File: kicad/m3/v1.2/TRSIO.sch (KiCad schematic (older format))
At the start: 25 parts, among them J1 TRS80, J2 +5V, J3 BUTTON, J4 LED, J5 FreHD Disable, J6 TRS80, Q1 2N7000, Q2 2N7000, Q3 2N7000, SW1 SW_Push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

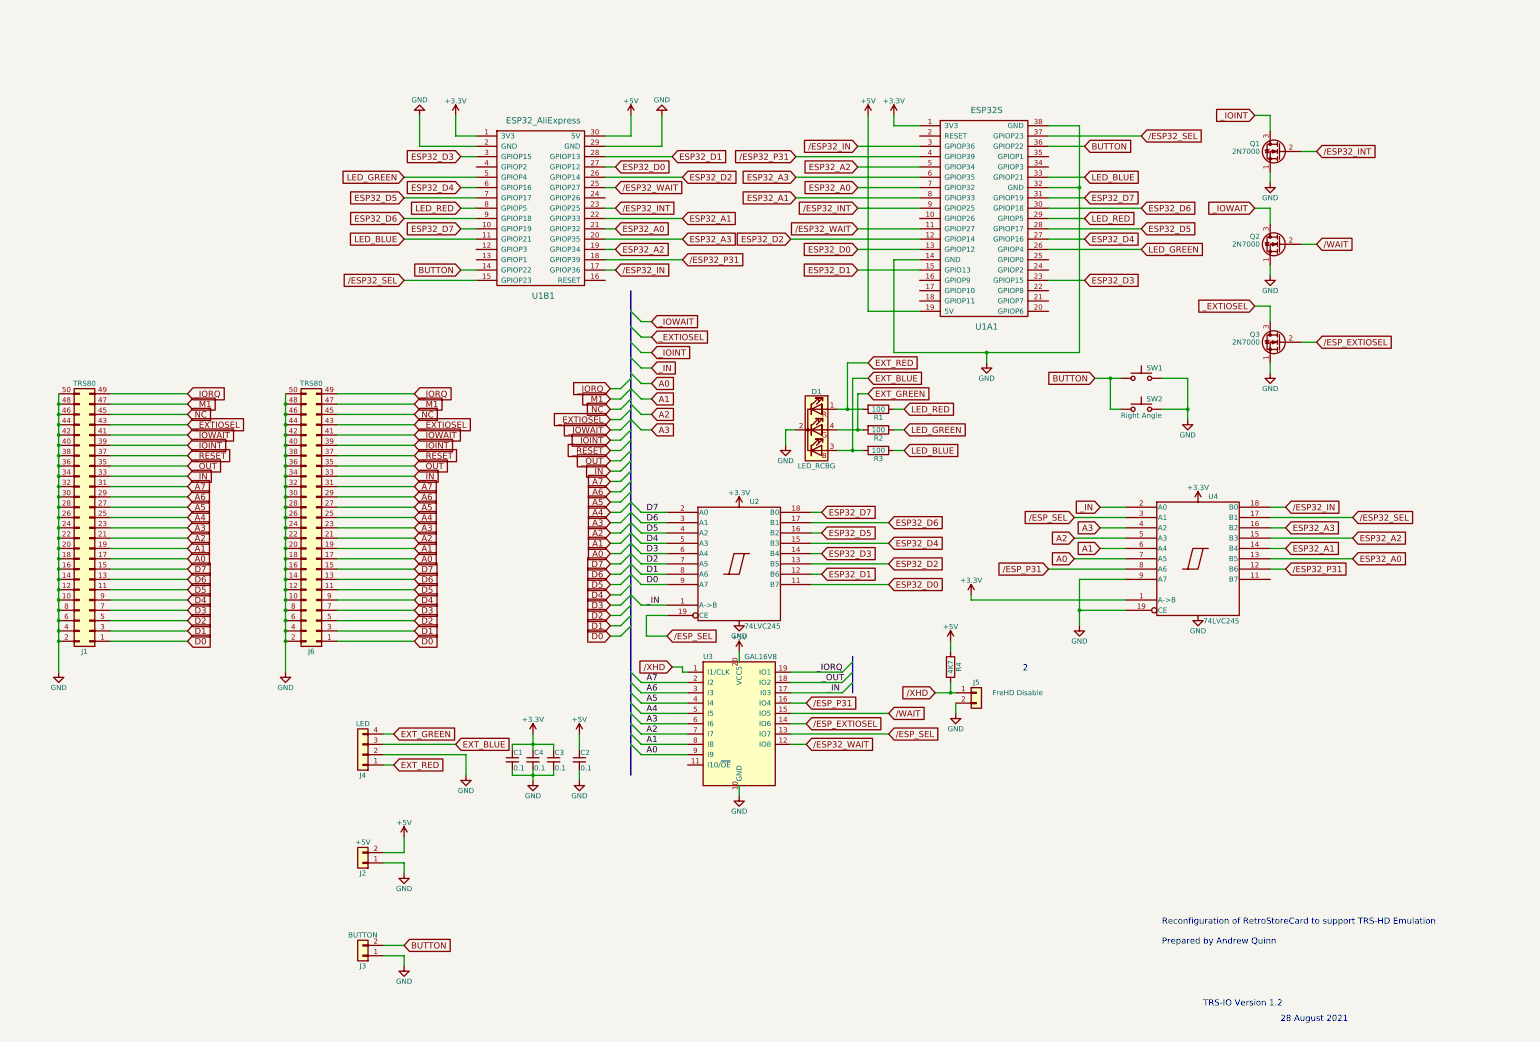
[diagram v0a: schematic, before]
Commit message: TRS-IO-M3 PCB v1.2 + SD Card
Schematic updates only.  PCB still outstanding
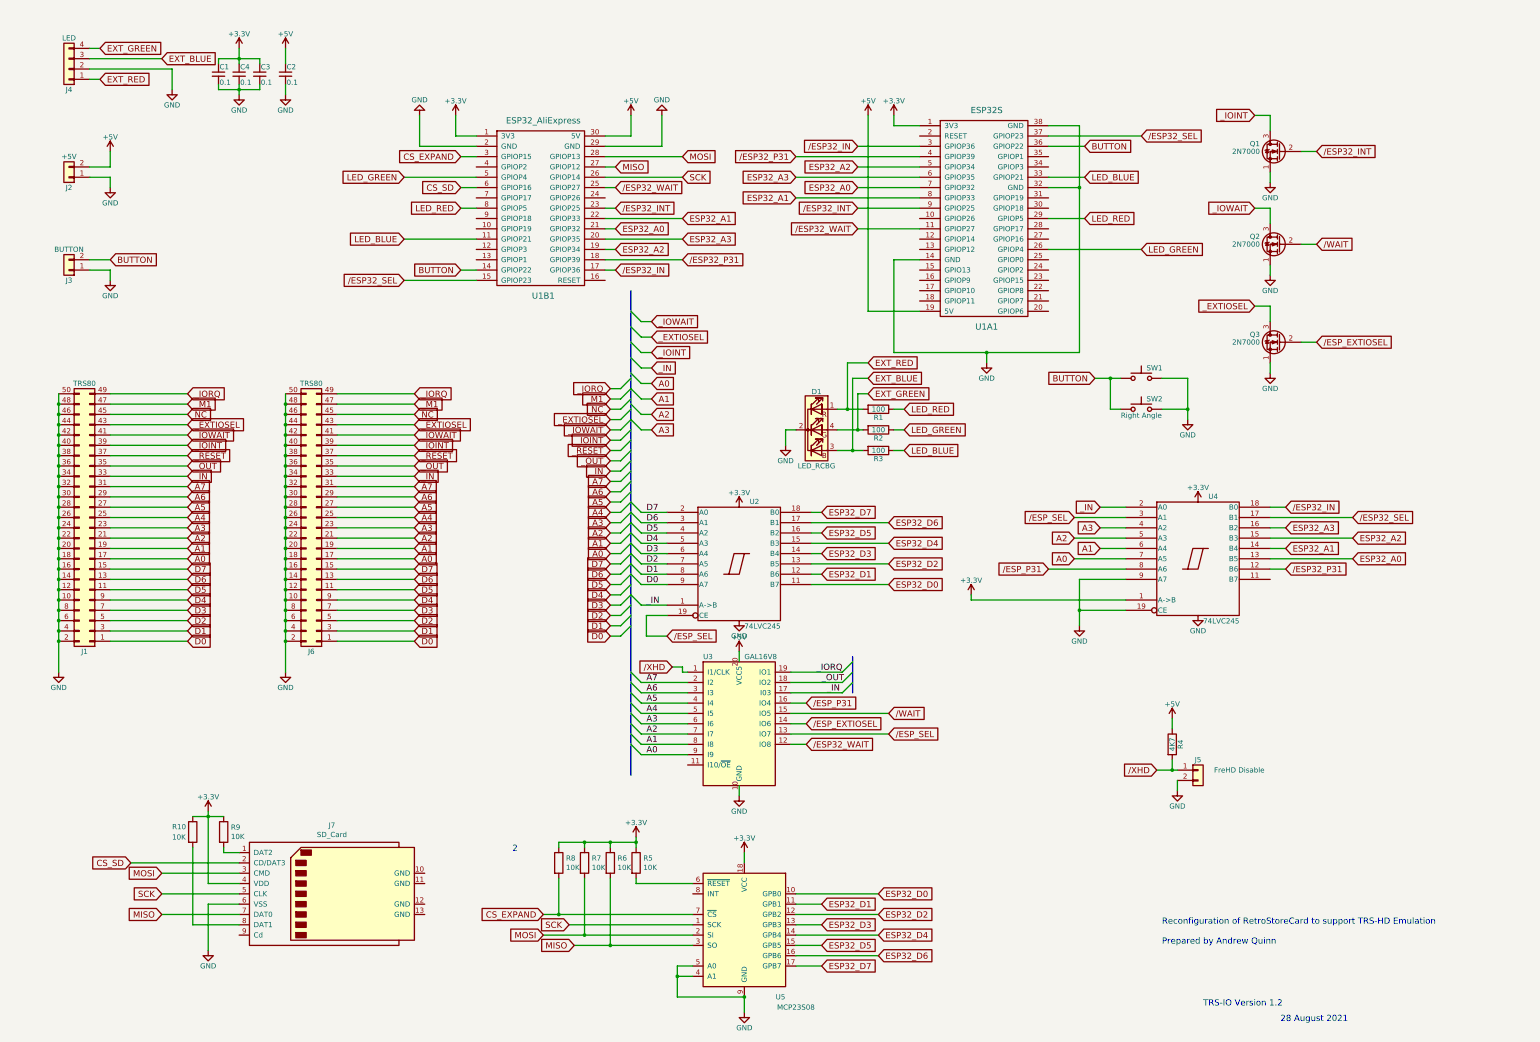
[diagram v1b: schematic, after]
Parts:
- added J7: SD_Card, symbol SDCard:SD_Card
- added R10, R5, R6, R7, R8, R9: 10K, symbol Device:R
- added U5: MCP23S08, symbol microchip:MCP23S08
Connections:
- net +3V3: now also J7.4 (VDD), R10.1, R5.1, R6.1, R7.1, R8.1, R9.1, U5.18 (VCC)
- net ESP32_D0: now also U5.10 (GPB0); no longer U1A1.13 (GPIOP12), U1B1.27 (GPIOP12)
- net ESP32_D1: now also U5.11 (GPB1); no longer U1A1.15 (GPIO13), U1B1.28 (GPIOP13)
- net ESP32_D2: now also U5.12 (GPB2); no longer U1A1.12 (GPIOP14), U1B1.26 (GPIOP14)
- net ESP32_D3: now also U5.13 (GPB3); no longer U1A1.23 (GPIOP15), U1B1.3 (GPIOP15)
- net ESP32_D4: now also U5.14 (GPB4); no longer U1A1.27 (GPIOP16), U1B1.6 (GPIOP16)
- net ESP32_D5: now also U5.15 (GPB5); no longer U1A1.28 (GPIOP17), U1B1.7 (GPIOP17)
- net ESP32_D6: now also U5.16 (GPB6); no longer U1A1.30 (GPIOP18), U1B1.9 (GPIOP18)
- net ESP32_D7: now also U5.17 (GPB7); no longer U1A1.31 (GPIOP19), U1B1.10 (GPIOP19)
- net GND: now also J7.6 (VSS), U5.4 (A1), U5.5 (A0), U5.9 (GND)
- new net: R5.2, U5.6 (~RESET)
- new net: J7.1 (DAT2), R9.2
- new net: J7.8 (DAT1), R10.2
- new net CS_EXPAND: R8.2, U1B1.3 (GPIOP15), U5.7 (~CS)
- new net CS_SD: J7.2 (CD/DAT3), U1B1.6 (GPIOP16)
- new net MISO: J7.7 (DAT0), R6.2, U1B1.27 (GPIOP12), U5.3 (SO)
- new net MOSI: J7.3 (CMD), R7.2, U1B1.28 (GPIOP13), U5.2 (SI)
- new net SCK: J7.5 (CLK), U1B1.26 (GPIOP14), U5.1 (SCK)
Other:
- moved on the sheet: C1, C2, C3, C4, J2, J3, J4, J5, R4

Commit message: TRS-IO-M3 PCB v1.2 + SD Card + PCB Updates
1. Connect GND pins of the SD card to ground
2. SPI pins connected for ESP32S
3. Pullup for CS_SD
4. PCB Layout
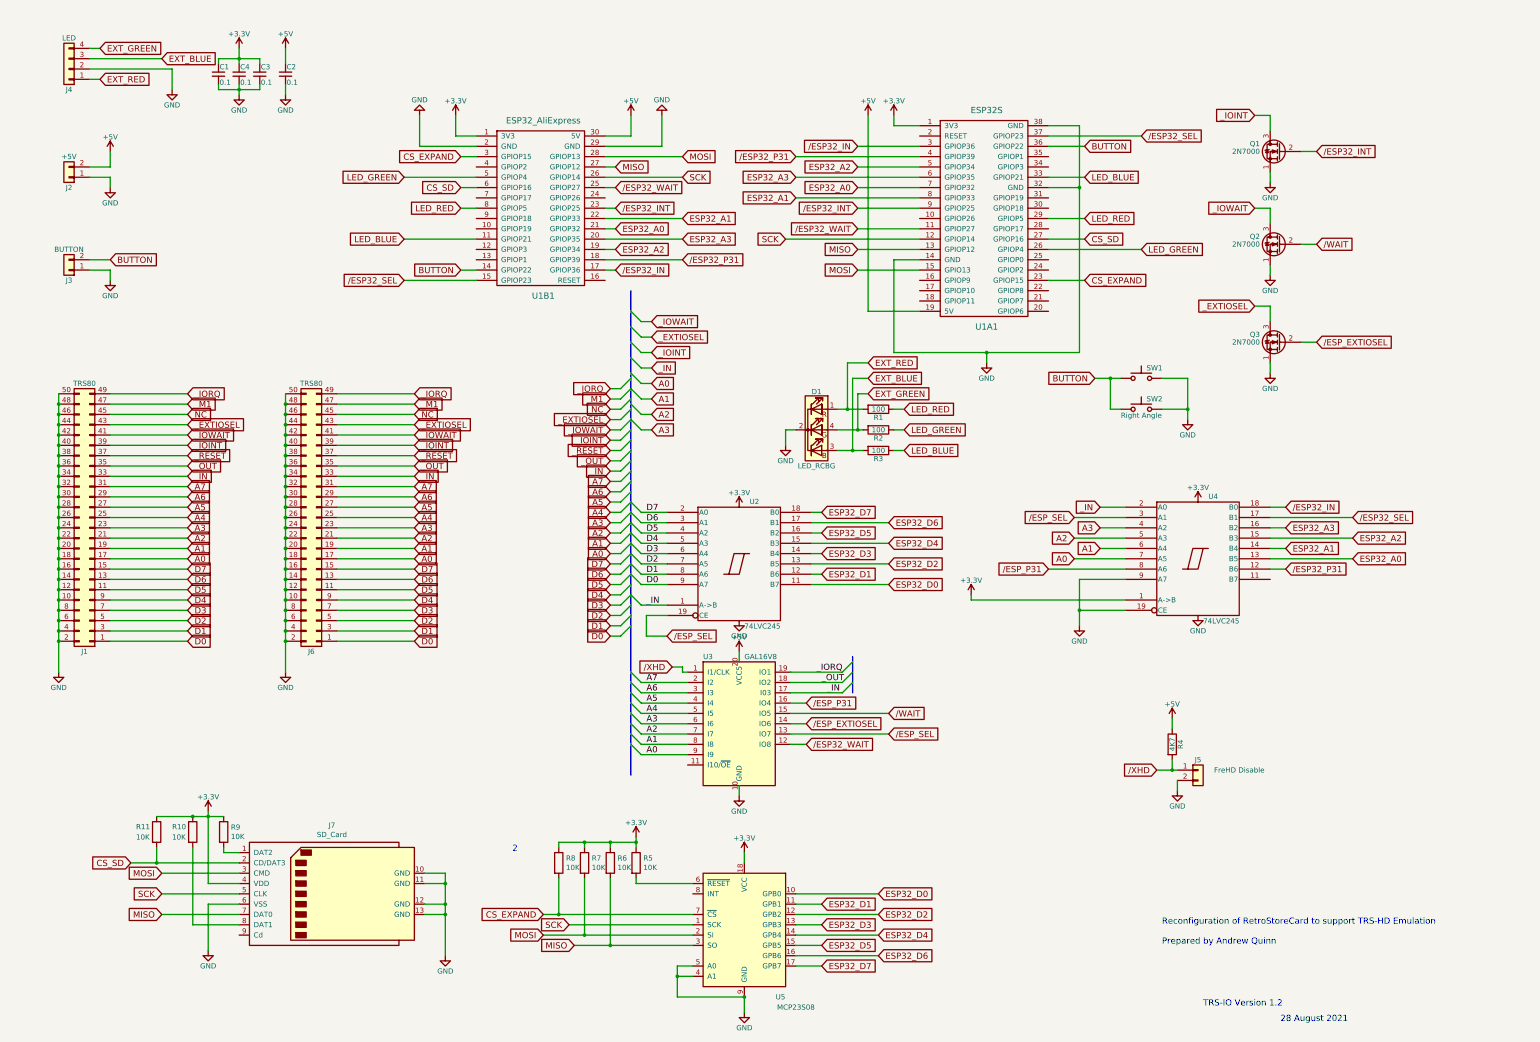
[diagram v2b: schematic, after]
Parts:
- added R11: 10K, Resistors_THT:R_Axial_DIN0207_L6.3mm_D2.5mm_P7.62mm_Horizontal, symbol Device:R
- J7: footprint (none) -> TRSIO:TFP09-2-12B
- R10, R5, R6, R7, R8, R9: footprint (none) -> Resistors_THT:R_Axial_DIN0207_L6.3mm_D2.5mm_P7.62mm_Horizontal
- U5: footprint (none) -> Housings_DIP:DIP-18_W7.62mm
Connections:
- net +3V3: now also R11.1
- net CS_EXPAND: now also U1A1.23 (GPIOP15)
- net CS_SD: now also U1A1.27 (GPIOP16), R11.2
- net GND: now also J7.10 (GND), J7.11 (GND), J7.12 (GND), J7.13 (GND)
- net MISO: now also U1A1.13 (GPIOP12)
- net MOSI: now also U1A1.15 (GPIO13)
- net SCK: now also U1A1.12 (GPIOP14)
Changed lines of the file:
@@
 F 0 "U5" H 7550 9400 50  0000 C CNN
 F 1 "MCP23S08" H 7400 9300 50  0000 C CNN
-F 2 "" H 7950 9450 50  0001 L CNN
+F 2 "Housings_DIP:DIP-18_W7.62mm" H 7950 9450 50  0001 L CNN
 F 3 "http://ww1.microchip.com/downloads/en/DeviceDoc/21919e.pdf" H 8150 10700 50  0001 C CNN
 	1    7900 10100
@@
 F 0 "R5" H 6920 9546 50  0000 L CNN
 F 1 "10K" H 6920 9455 50  0000 L CNN
-F 2 "" V 6780 9500 50  0001 C CNN
+F 2 "Resistors_THT:R_Axial_DIN0207_L6.3mm_D2.5mm_P7.62mm_Horizontal" V 6780 9500 50  0001 C CNN
 F 3 "~" H 6850 9500 50  0001 C CNN
 	1    6850 9500
@@
 F 0 "R6" H 6670 9546 50  0000 L CNN
 F 1 "10K" H 6670 9455 50  0000 L CNN
-F 2 "" V 6530 9500 50  0001 C CNN
+F 2 "Resistors_THT:R_Axial_DIN0207_L6.3mm_D2.5mm_P7.62mm_Horizontal" V 6530 9500 50  0001 C CNN
 F 3 "~" H 6600 9500 50  0001 C CNN
 	1    6600 9500
@@
 F 0 "R7" H 6420 9546 50  0000 L CNN
 F 1 "10K" H 6420 9455 50  0000 L CNN
-F 2 "" V 6280 9500 50  0001 C CNN
+F 2 "Resistors_THT:R_Axial_DIN0207_L6.3mm_D2.5mm_P7.62mm_Horizontal" V 6280 9500 50  0001 C CNN
 F 3 "~" H 6350 9500 50  0001 C CNN
 	1    6350 9500
@@
 F 0 "R8" H 6170 9546 50  0000 L CNN
 F 1 "10K" H 6170 9455 50  0000 L CNN
-F 2 "" V 6030 9500 50  0001 C CNN
+F 2 "Resistors_THT:R_Axial_DIN0207_L6.3mm_D2.5mm_P7.62mm_Horizontal" V 6030 9500 50  0001 C CNN
 F 3 "~" H 6100 9500 50  0001 C CNN
 	1    6100 9500
@@
 F 0 "J7" H 3900 10465 50  0000 C CNN
 F 1 "SD_Card" H 3900 10374 50  0000 C CNN
-F 2 "" H 3900 9800 50  0001 C CNN
+F 2 "TRSIO:TFP09-2-12B" H 3900 9800 50  0001 C CNN
 F 3 "http://portal.fciconnect.com/Comergent//fci/drawing/10067847.pdf" H 3900 9800 50  0001 C CNN
 	1    3900 9800
@@
 F 0 "R9" H 2920 9246 50  0000 L CNN
 F 1 "10K" H 2920 9155 50  0000 L CNN
-F 2 "" V 2780 9200 50  0001 C CNN
+F 2 "Resistors_THT:R_Axial_DIN0207_L6.3mm_D2.5mm_P7.62mm_Horizontal" V 2780 9200 50  0001 C CNN
 F 3 "~" H 2850 9200 50  0001 C CNN
 	1    2850 9200
@@
 SCK
 Wire Wire Line
-	1950 9500 3000 9500
+	1950 9500 2200 9500
 Wire Wire Line
 	2250 9600 3000 9600
@@
 F 0 "R10" H 2350 9250 50  0000 L CNN
 F 1 "10K" H 2350 9150 50  0000 L CNN
-F 2 "" V 2480 9200 50  0001 C CNN
+F 2 "Resistors_THT:R_Axial_DIN0207_L6.3mm_D2.5mm_P7.62mm_Horizontal" V 2480 9200 50  0001 C CNN
 F 3 "~" H 2550 9200 50  0001 C CNN
 	1    2550 9200
@@
 Wire Wire Line
 	2700 9900 2700 10350
+Text GLabel 11200 3850 2    60   Input ~ 0
+CS_EXPAND
+Wire Wire Line
+	10850 3850 11200 3850
+Text GLabel 11200 3450 2    60   Input ~ 0
+CS_SD
+Wire Wire Line
+	11200 3450 10850 3450
+Text GLabel 9000 3750 0    60   Input ~ 0
+MOSI
+Wire Wire Line
+	9600 3750 9000 3750
+Text GLabel 9000 3550 0    60   Input ~ 0
+MISO
+Wire Wire Line
+	9000 3550 9600 3550
+Text GLabel 8300 3450 0    60   Input ~ 0
+SCK
+Wire Wire Line
+	8300 3450 9600 3450
+$Comp
+L Device:R R11
+U 1 1 61473039
+P 2200 9200
+F 0 "R11" H 2000 9250 50  0000 L CNN
+F 1 "10K" H 2000 9150 50  0000 L CNN
+F 2 "Resistors_THT:R_Axial_DIN0207_L6.3mm_D2.5mm_P7.62mm_Horizontal" V 2130 9200 50  0001 C CNN
+F 3 "~" H 2200 9200 50  0001 C CNN
+	1    2200 9200
+	1    0    0    -1
+$EndComp
+Wire Wire Line
+	2200 9050 2550 9050
+Connection ~ 2550 9050
+Wire Wire Line
+	2200 9350 2200 9500
+Connection ~ 2200 9500
+Wire Wire Line
+	2200 9500 3000 9500
+$Comp
+L power:GND #PWR?
+U 1 1 614CC471
+P 5000 10400
+F 0 "#PWR?" H 5000 10150 50  0001 C CNN
+F 1 "GND" H 5000 10250 50  0000 C CNN
+F 2 "" H 5000 10400 50  0001 C CNN
+F 3 "" H 5000 10400 50  0001 C CNN
+	1    5000 10400
+	1    0    0    -1
+$EndComp
+Wire Wire Line
+	4800 9600 5000 9600
+Wire Wire Line
+	5000 9600 5000 9700
+Wire Wire Line
+	4800 9700 5000 9700
+Connection ~ 5000 9700
+Wire Wire Line
+	5000 9700 5000 9900
+Wire Wire Line
+	4800 9900 5000 9900
+Connection ~ 5000 9900
+Wire Wire Line
+	5000 9900 5000 10000
+Wire Wire Line
+	4800 10000 5000 10000
 Wire Bus Line
 	8950 7500 8950 7850
 Wire Bus Line
 	6800 3950 6800 8650
+Connection ~ 5000 10000
+Wire Wire Line
+	5000 10000 5000 10400
 $EndSCHEMATC

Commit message: TRS-IO-M3 PCB v1.2 + SD Card + PCB Updates
1. Updated labels for buffered data bus signals from ESP32_Dx to BDx.
2. Updated meta data on schematic and PCB
3. Added M3 mounting holes to PCB
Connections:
- net ESP32_D0 renamed BD0
- net ESP32_D1 renamed BD1
- net ESP32_D2 renamed BD2
- net ESP32_D3 renamed BD3
- net ESP32_D4 renamed BD4
- net ESP32_D5 renamed BD5
- net ESP32_D6 renamed BD6
- net ESP32_D7 renamed BD7
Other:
- note added: "Updated TRS-IO with SD Card Support and Edge Connector"
- note removed: "Reconfiguration of RetroStoreCard to support TRS-HD Emulation\n\nPrepared by Andrew Quinn"
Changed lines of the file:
@@
 $EndComp
 Text GLabel 8650 6100 2    60   Input ~ 0
-ESP32_D7
+BD7
 Text GLabel 8650 6300 2    60   Input ~ 0
-ESP32_D5
+BD5
 Text GLabel 8650 6500 2    60   Input ~ 0
-ESP32_D3
+BD3
 Text GLabel 8650 6700 2    60   Input ~ 0
-ESP32_D1
+BD1
 Text GLabel 9300 6200 2    60   Input ~ 0
-ESP32_D6
+BD6
 Text GLabel 9300 6400 2    60   Input ~ 0
-ESP32_D4
+BD4
 Text GLabel 9300 6600 2    60   Input ~ 0
-ESP32_D2
+BD2
 Text GLabel 9300 6800 2    60   Input ~ 0
-ESP32_D0
+BD0
 Text GLabel 11750 2450 2    60   Input ~ 0
 /ESP32_SEL
@@
 Entry Wire Line
 	6800 4600 6900 4700
-Text Notes 11950 10300 0    60   ~ 0
-Reconfiguration of RetroStoreCard to support TRS-HD Emulation\n\nPrepared by Andrew Quinn
+Text Notes 11900 10150 0    60   ~ 0
+Updated TRS-IO with SD Card Support and Edge Connector
 Text Notes 13100 11050 0    60   ~ 0
 28 August 2021
@@
 $EndComp
 Text GLabel 9200 9800 2    60   Input ~ 0
-ESP32_D0
+BD0
 Text GLabel 8650 9900 2    60   Input ~ 0
-ESP32_D1
+BD1
 Text GLabel 9200 10000 2    60   Input ~ 0
-ESP32_D2
+BD2
 Text GLabel 8650 10100 2    60   Input ~ 0
-ESP32_D3
+BD3
 Text GLabel 9200 10200 2    60   Input ~ 0
-ESP32_D4
+BD4
 Text GLabel 8650 10300 2    60   Input ~ 0
-ESP32_D5
+BD5
 Text GLabel 9200 10400 2    60   Input ~ 0
-ESP32_D6
+BD6
 Wire Wire Line
 	8400 9800 9200 9800
@@
 	8400 10400 9200 10400
 Text GLabel 8650 10500 2    60   Input ~ 0
-ESP32_D7
+BD7
 Wire Wire Line
 	8400 10500 8650 10500
@@
 Wire Wire Line
 	4800 10000 5000 10000
+Connection ~ 5000 10000
+Wire Wire Line
+	5000 10000 5000 10400
 Wire Bus Line
 	8950 7500 8950 7850
 Wire Bus Line
 	6800 3950 6800 8650
-Connection ~ 5000 10000
-Wire Wire Line
-	5000 10000 5000 10400
 $EndSCHEMATC

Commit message: Fix incorrect schematic references after Kicad upgrade
Corrections to the following invalid schematic symbol references:
1. 2N7000
2. SW_Push
3. MCP23S08
4. Conn_01x02
5. Conn_01x04
6. Conn_02x25_Odd_Even
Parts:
- J1, J6: symbol conn:Conn_02x25_Odd_Even -> Connector_Generic:Conn_02x25_Odd_Even
- J2, J3, J5: symbol conn:Conn_01x02 -> Connector_Generic:Conn_01x02
- J4: symbol conn:Conn_01x04 -> Connector_Generic:Conn_01x04
- Q1, Q2, Q3: symbol transistors:2N7000 -> Transistor_FET:2N7000
- SW1, SW2: symbol switches:SW_Push -> Switch:SW_Push
- U5: symbol microchip:MCP23S08 -> TRSIO:MCP23S08-microchip
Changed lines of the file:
@@
 /ESP_SEL
 $Comp
-L conn:Conn_02x25_Odd_Even J1
+L Connector_Generic:Conn_02x25_Odd_Even J1
 U 1 1 5C5A156A
 P 1550 6150
@@
 $EndComp
 $Comp
-L transistors:2N7000 Q1
+L Transistor_FET:2N7000 Q1
 U 1 1 5C5B476F
 P 13100 2600
@@
 /ESP32_INT
 $Comp
-L switches:SW_Push SW1
+L Switch:SW_Push SW1
 U 1 1 5C5CC661
 P 11750 4800
@@
 $EndComp
 $Comp
-L transistors:2N7000 Q3
+L Transistor_FET:2N7000 Q3
 U 1 1 5CCC1D78
 P 13100 4450
@@
 $EndComp
 $Comp
-L transistors:2N7000 Q2
+L Transistor_FET:2N7000 Q2
 U 1 1 5CCC1E34
 P 13100 3500
@@
 $EndComp
 $Comp
-L conn:Conn_01x02 J2
+L Connector_Generic:Conn_01x02 J2
 U 1 1 5D04909B
 P 1350 2850
@@
 	1750 2850 1750 2950
 $Comp
-L conn:Conn_01x02 J3
+L Connector_Generic:Conn_01x02 J3
 U 1 1 5D04AF05
 P 1350 3750
@@
 	1550 3650 1750 3650
 $Comp
-L conn:Conn_01x04 J4
+L Connector_Generic:Conn_01x04 J4
 U 1 1 5D04CE51
 P 1350 1800
@@
 Connection ~ 8900 5100
 $Comp
-L switches:SW_Push SW2
+L Switch:SW_Push SW2
 U 1 1 5D0574E5
 P 11750 5100
@@
 $EndComp
 $Comp
-L conn:Conn_01x02 J5
+L Connector_Generic:Conn_01x02 J5
 U 1 1 5DE379E9
 P 12300 8600
@@
 D0
 $Comp
-L conn:Conn_02x25_Odd_Even J6
+L Connector_Generic:Conn_02x25_Odd_Even J6
 U 1 1 612D58A9
 P 3750 6150
@@
 	6600 7300 6700 7300
 $Comp
-L microchip:MCP23S08 U5
+L TRSIO:MCP23S08-microchip U5
 U 1 1 612D1A51
 P 7900 10100
